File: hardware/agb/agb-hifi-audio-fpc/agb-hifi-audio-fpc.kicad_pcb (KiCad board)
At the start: 2 copper layers, 23.1 x 34.8 mm, 4 parts, among them J1 AGB_AMP_CONNECT, J4 PAIR, J5 BOARD_CONNECT

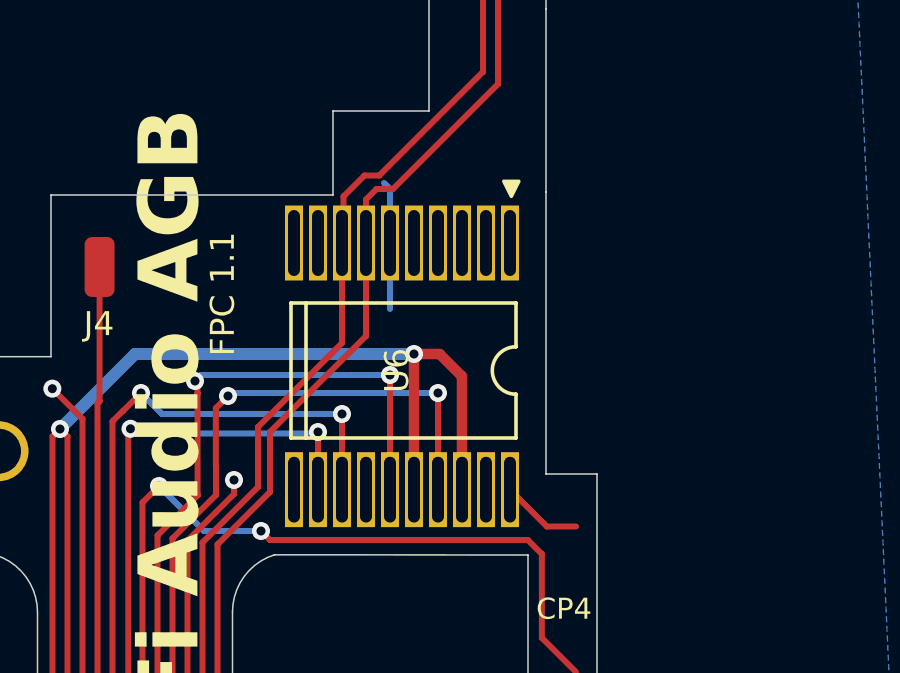
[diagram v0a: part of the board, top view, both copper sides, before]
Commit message: hardware(agb): move the GND ties near the U6 slots to F.Cu, loosen the zone fill
Board-side layout change made in KiCad: drop three B.Cu GND segments around
x=94.3 (y 100.2-104.4) and run GND on F.Cu instead, with new stitching vias
(0.6/0.3) at (94.3, 104.175) and (98.3, 108.475). The GND zone's min_thickness
goes 0.25 -> 0.1 mm and connect_pads clearance 0.5 -> 0.1 mm so the pour reaches
into the tighter gaps; zone defaults in the .kicad_pro follow. DRC clean.
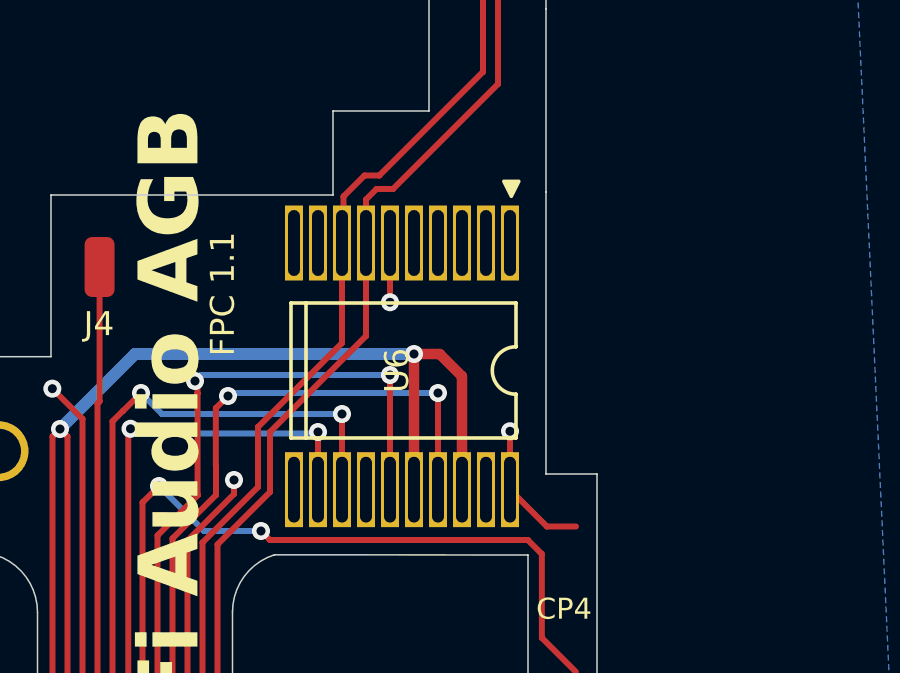
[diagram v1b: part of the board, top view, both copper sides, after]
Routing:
- net GND: track 38.9 -> 38.5 mm, vias 2 -> 4
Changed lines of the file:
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@@
 			(size 2.5 0.6)
 			(drill oval 2.2 0.4)
-			(layers "*.Cu" "*.Mask" "F.Paste")
+			(layers "*.Cu" "F.Mask" "F.Paste")
 			(remove_unused_layers no)
 			(net "unconnected-(J1-Pin_1-Pad1)")
@@
 			(size 2.5 0.6)
 			(drill oval 2.2 0.4)
-			(layers "*.Cu" "*.Mask" "F.Paste")
+			(layers "*.Cu" "F.Mask" "F.Paste")
 			(remove_unused_layers no)
 			(net "unconnected-(J1-Pin_1-Pad1)_1")
@@
 			(size 2.5 0.6)
 			(drill oval 2.2 0.4)
-			(layers "*.Cu" "*.Mask" "F.Paste")
+			(layers "*.Cu" "F.Mask" "F.Paste")
 			(remove_unused_layers no)
 			(net "unconnected-(J1-Pin_1-Pad1)_2")
@@
 			(size 2.5 0.6)
 			(drill oval 2.2 0.4)
-			(layers "*.Cu" "*.Mask" "F.Paste")
+			(layers "*.Cu" "F.Mask" "F.Paste")
 			(remove_unused_layers no)
 			(net "unconnected-(J1-Pin_2-Pad2)")
@@
 			(size 2.5 0.6)
 			(drill oval 2.2 0.4)
-			(layers "*.Cu" "*.Mask" "F.Paste")
+			(layers "*.Cu" "F.Mask" "F.Paste")
 			(remove_unused_layers no)
 			(net "unconnected-(J1-Pin_3-Pad3)")
@@
 			(size 2.5 0.6)
 			(drill oval 2.2 0.4)
-			(layers "*.Cu" "*.Mask" "F.Paste")
+			(layers "*.Cu" "F.Mask" "F.Paste")
 			(remove_unused_layers no)
 			(net "unconnected-(J1-Pin_4-Pad4)")
@@
 			(size 2.5 0.6)
 			(drill oval 2.2 0.4)
-			(layers "*.Cu" "*.Mask" "F.Paste")
+			(layers "*.Cu" "F.Mask" "F.Paste")
 			(remove_unused_layers no)
 			(net "unconnected-(J1-Pin_5-Pad5)")
@@
 			(size 2.5 0.6)
 			(drill oval 2.2 0.4)
-			(layers "*.Cu" "*.Mask" "F.Paste")
+			(layers "*.Cu" "F.Mask" "F.Paste")
 			(remove_unused_layers no)
 			(net "GND")
@@
 			(size 2.5 0.6)
 			(drill oval 2.2 0.4)
-			(layers "*.Cu" "*.Mask" "F.Paste")
+			(layers "*.Cu" "F.Mask" "F.Paste")
 			(remove_unused_layers no)
 			(net "RIN")
@@
 			(size 2.5 0.6)
 			(drill oval 2.2 0.4)
-			(layers "*.Cu" "*.Mask" "F.Paste")
+			(layers "*.Cu" "F.Mask" "F.Paste")
 			(remove_unused_layers no)
 			(net "LIN")
@@
 			(size 2.5 0.6)
 			(drill oval 2.2 0.4)
-			(layers "*.Cu" "*.Mask" "F.Paste")
+			(layers "*.Cu" "F.Mask" "F.Paste")
 			(remove_unused_layers no)
 			(net "unconnected-(J1-Pin_9-Pad9)")
@@
 			(size 2.5 0.6)
 			(drill oval 2.2 0.4)
-			(layers "*.Cu" "*.Mask" "F.Paste")
+			(layers "*.Cu" "F.Mask" "F.Paste")
 			(remove_unused_layers no)
 			(net "VOL")
@@
 			(size 2.5 0.6)
 			(drill oval 2.2 0.4)
-			(layers "*.Cu" "*.Mask" "F.Paste")
+			(layers "*.Cu" "F.Mask" "F.Paste")
 			(remove_unused_layers no)
 			(net "SW")
@@
 			(size 2.5 0.6)
 			(drill oval 2.2 0.4)
-			(layers "*.Cu" "*.Mask" "F.Paste")
+			(layers "*.Cu" "F.Mask" "F.Paste")
 			(remove_unused_layers no)
 			(net "unconnected-(J1-Pin_12-Pad12)")
@@
 			(size 2.5 0.6)
 			(drill oval 2.2 0.4)
-			(layers "*.Cu" "*.Mask" "F.Paste")
+			(layers "*.Cu" "F.Mask" "F.Paste")
 			(remove_unused_layers no)
 			(net "LOUT")
@@
 			(size 2.5 0.6)
 			(drill oval 2.2 0.4)
-			(layers "*.Cu" "*.Mask" "F.Paste")
+			(layers "*.Cu" "F.Mask" "F.Paste")
 			(remove_unused_layers no)
 			(net "VBAT")
@@
 			(size 2.5 0.6)
 			(drill oval 2.2 0.4)
-			(layers "*.Cu" "*.Mask" "F.Paste")
+			(layers "*.Cu" "F.Mask" "F.Paste")
 			(remove_unused_layers no)
 			(net "ROUT")
@@
 			(size 2.5 0.6)
 			(drill oval 2.2 0.4)
-			(layers "*.Cu" "*.Mask" "F.Paste")
+			(layers "*.Cu" "F.Mask" "F.Paste")
 			(remove_unused_layers no)
 			(net "VBAT")
@@
 			(size 2.5 0.6)
 			(drill oval 2.2 0.4)
-			(layers "*.Cu" "*.Mask" "F.Paste")
+			(layers "*.Cu" "F.Mask" "F.Paste")
 			(remove_unused_layers no)
 			(net "unconnected-(J1-Pin_17-Pad17)")
@@
 			(size 2.5 0.6)
 			(drill oval 2.2 0.4)
-			(layers "*.Cu" "*.Mask" "F.Paste")
+			(layers "*.Cu" "F.Mask" "F.Paste")
 			(remove_unused_layers no)
 			(net "GND")
@@
 	)
 	(segment
+		(start 94.3 102.2)
+		(end 94.3 104.175)
+		(width 0.2)
+		(layer "F.Cu")
+		(net "GND")
+	)
+	(segment
 		(start 87.55 112.118628)
 		(end 87.55 124)
@@
 	)
 	(segment
+		(start 98.3 108.475)
+		(end 98.3 110.42132)
+		(width 0.2)
+		(layer "F.Cu")
+		(net "GND")
+	)
+	(segment
 		(start 87.55 112.118628)
 		(end 89.1 110.568628)
@@
 	)
 	(via
-		(at 83.044975 107.055025)
+		(at 98.3 108.475)
 		(size 0.6)
 		(drill 0.3)
@@
 	)
 	(via
-		(at 89.1 110.1)
+		(at 83.044975 107.055025)
 		(size 0.6)
 		(drill 0.3)
@@
 		(net "GND")
 	)
-	(segment
-		(start 94.3 102.2)
-		(end 94.3 104.4)
-		(width 0.2)
-		(layer "B.Cu")
-		(net "GND")
-	)
-	(segment
-		(start 94.1 100.2)
-		(end 94.3 100.4)
-		(width 0.2)
-		(layer "B.Cu")
+	(via
+		(at 89.1 110.1)
+		(size 0.6)
+		(drill 0.3)
+		(layers "F.Cu" "B.Cu")
 		(net "GND")
 	)
-	(segment
-		(start 94.3 100.4)
-		(end 94.3 102.2)
-		(width 0.2)
-		(layer "B.Cu")
+	(via
+		(at 94.3 104.175)
+		(size 0.6)
+		(drill 0.3)
+		(layers "F.Cu" "B.Cu")
+		(free yes)
 		(net "GND")
 	)
@@
 		(hatch edge 0.5)
 		(connect_pads
-			(clearance 0.5)
+			(clearance 0.1)
 		)
-		(min_thickness 0.25)
+		(min_thickness 0.1)
 		(fill yes
 			(thermal_gap 0.5)
